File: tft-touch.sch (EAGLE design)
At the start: 4 parts

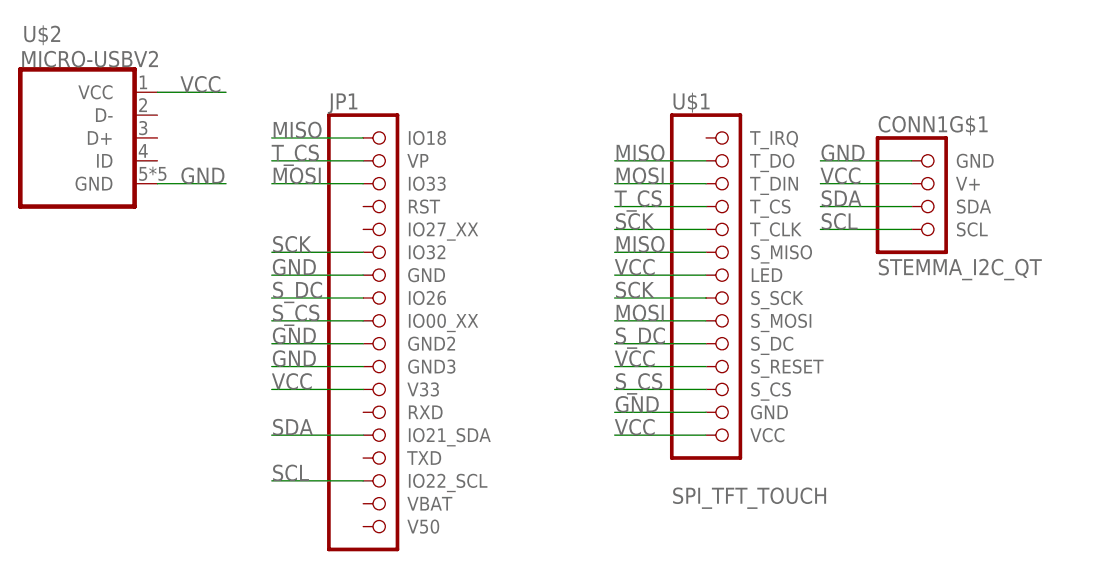
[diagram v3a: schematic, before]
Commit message: Enlarged usb pin holes
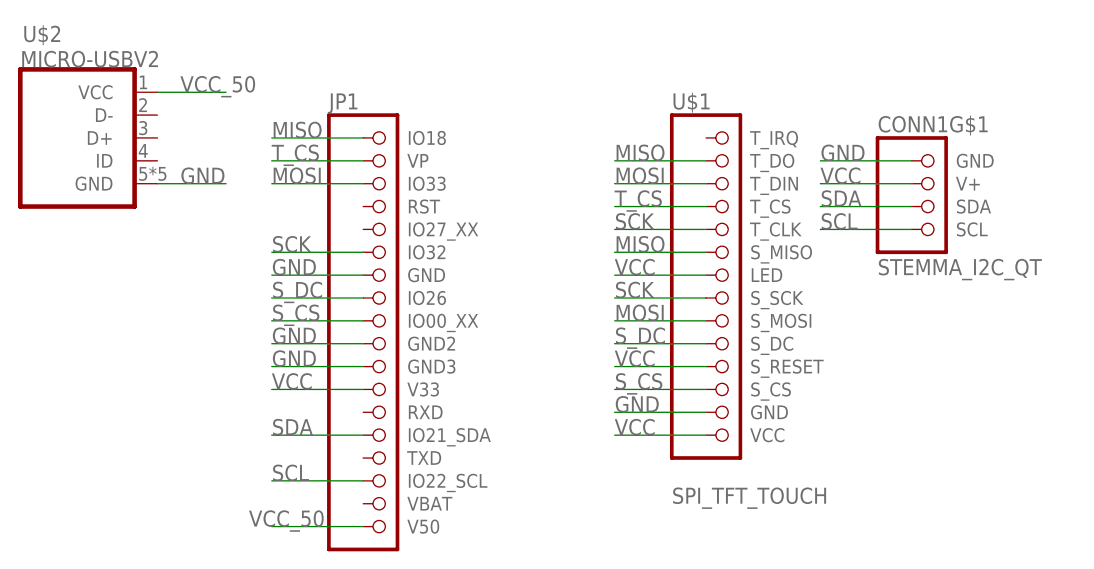
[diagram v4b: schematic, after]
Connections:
- new net VCC_50: JP1.V50, U$2.VCC
- net VCC: no longer U$2.VCC

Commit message: Fix USB connector dimensions
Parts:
- U$2: device microusb:MICRO-USBV2 -> 01jim:MICRO-USBV2
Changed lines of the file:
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@@
 <grid distance="0.1" unitdist="inch" unit="inch" style="lines" multiple="1" display="no" altdistance="0.01" altunitdist="inch" altunit="inch"/>
 <layers>
-<layer number="1" name="Top" color="4" fill="1" visible="yes" active="no"/>
-<layer number="16" name="Bottom" color="1" fill="1" visible="yes" active="no"/>
-<layer number="17" name="Pads" color="2" fill="1" visible="yes" active="no"/>
-<layer number="18" name="Vias" color="2" fill="1" visible="yes" active="no"/>
-<layer number="19" name="Unrouted" color="6" fill="1" visible="yes" active="no"/>
-<layer number="20" name="Dimension" color="24" fill="1" visible="yes" active="no"/>
-<layer number="21" name="tPlace" color="7" fill="1" visible="yes" active="no"/>
-<layer number="22" name="bPlace" color="7" fill="1" visible="yes" active="no"/>
-<layer number="23" name="tOrigins" color="15" fill="1" visible="yes" active="no"/>
-<layer number="24" name="bOrigins" color="15" fill="1" visible="yes" active="no"/>
-<layer number="25" name="tNames" color="7" fill="1" visible="yes" active="no"/>
-<layer number="26" name="bNames" color="7" fill="1" visible="yes" active="no"/>
-<layer number="27" name="tValues" color="7" fill="1" visible="yes" active="no"/>
-<layer number="28" name="bValues" color="7" fill="1" visible="yes" active="no"/>
+<layer number="1" name="Top" color="4" fill="1" visible="no" active="no"/>
+<layer number="16" name="Bottom" color="1" fill="1" visible="no" active="no"/>
+<layer number="17" name="Pads" color="2" fill="1" visible="no" active="no"/>
+<layer number="18" name="Vias" color="2" fill="1" visible="no" active="no"/>
+<layer number="19" name="Unrouted" color="6" fill="1" visible="no" active="no"/>
+<layer number="20" name="Dimension" color="24" fill="1" visible="no" active="no"/>
+<layer number="21" name="tPlace" color="7" fill="1" visible="no" active="no"/>
+<layer number="22" name="bPlace" color="7" fill="1" visible="no" active="no"/>
+<layer number="23" name="tOrigins" color="15" fill="1" visible="no" active="no"/>
+<layer number="24" name="bOrigins" color="15" fill="1" visible="no" active="no"/>
+<layer number="25" name="tNames" color="7" fill="1" visible="no" active="no"/>
+<layer number="26" name="bNames" color="7" fill="1" visible="no" active="no"/>
+<layer number="27" name="tValues" color="7" fill="1" visible="no" active="no"/>
+<layer number="28" name="bValues" color="7" fill="1" visible="no" active="no"/>
 <layer number="29" name="tStop" color="7" fill="3" visible="no" active="no"/>
 <layer number="30" name="bStop" color="7" fill="6" visible="no" active="no"/>
@@
 <layer number="35" name="tGlue" color="7" fill="4" visible="no" active="no"/>
 <layer number="36" name="bGlue" color="7" fill="5" visible="no" active="no"/>
-<layer number="37" name="tTest" color="7" fill="1" visible="yes" active="no"/>
-<layer number="38" name="bTest" color="7" fill="1" visible="yes" active="no"/>
+<layer number="37" name="tTest" color="7" fill="1" visible="no" active="no"/>
+<layer number="38" name="bTest" color="7" fill="1" visible="no" active="no"/>
 <layer number="39" name="tKeepout" color="4" fill="11" visible="no" active="no"/>
 <layer number="40" name="bKeepout" color="1" fill="11" visible="no" active="no"/>
@@
 <layer number="44" name="Drills" color="7" fill="1" visible="no" active="no"/>
 <layer number="45" name="Holes" color="7" fill="1" visible="no" active="no"/>
-<layer number="46" name="Milling" color="3" fill="1" visible="yes" active="no"/>
-<layer number="47" name="Measures" color="7" fill="1" visible="yes" active="no"/>
-<layer number="48" name="Document" color="7" fill="1" visible="yes" active="no"/>
-<layer number="49" name="Reference" color="7" fill="1" visible="yes" active="no"/>
-<layer number="50" name="dxf" color="7" fill="1" visible="yes" active="no"/>
-<layer number="51" name="tDocu" color="7" fill="1" visible="yes" active="no"/>
-<layer number="52" name="bDocu" color="7" fill="1" visible="yes" active="no"/>
-<layer number="53" name="tGND_GNDA" color="7" fill="9" visible="yes" active="no"/>
-<layer number="54" name="bGND_GNDA" color="1" fill="9" visible="yes" active="no"/>
-<layer number="56" name="wert" color="7" fill="1" visible="yes" active="no"/>
-<layer number="57" name="tCAD" color="7" fill="1" visible="yes" active="no"/>
-<layer number="58" name="b3D" color="7" fill="1" visible="yes" active="no"/>
-<layer number="59" name="tCarbon" color="7" fill="1" visible="yes" active="no"/>
-<layer number="60" name="bCarbon" color="7" fill="1" visible="yes" active="no"/>
-<layer number="61" name="stand" color="7" fill="1" visible="yes" active="no"/>
+<layer number="46" name="Milling" color="3" fill="1" visible="no" active="no"/>
+<layer number="47" name="Measures" color="7" fill="1" visible="no" active="no"/>
+<layer number="48" name="Document" color="7" fill="1" visible="no" active="no"/>
+<layer number="49" name="Reference" color="7" fill="1" visible="no" active="no"/>
+<layer number="50" name="dxf" color="7" fill="1" visible="no" active="no"/>
+<layer number="51" name="tDocu" color="7" fill="1" visible="no" active="no"/>
+<layer number="52" name="bDocu" color="7" fill="1" visible="no" active="no"/>
+<layer number="53" name="tGND_GNDA" color="7" fill="9" visible="no" active="no"/>
+<layer number="54" name="bGND_GNDA" color="1" fill="9" visible="no" active="no"/>
+<layer number="56" name="wert" color="7" fill="1" visible="no" active="no"/>
+<layer number="57" name="tCAD" color="7" fill="1" visible="no" active="no"/>
+<layer number="58" name="b3D" color="7" fill="1" visible="no" active="no"/>
+<layer number="59" name="tCarbon" color="7" fill="1" visible="no" active="no"/>
+<layer number="60" name="bCarbon" color="7" fill="1" visible="no" active="no"/>
+<layer number="61" name="stand" color="7" fill="1" visible="no" active="no"/>
 <layer number="88" name="SimResults" color="9" fill="1" visible="yes" active="yes"/>
 <layer number="89" name="SimProbes" color="9" fill="1" visible="yes" active="yes"/>
@@
 <part name="JP1" library="00jim" deviceset="TTGO-TS-ESP32" device=""/>
 <part name="CONN1" library="00jim" deviceset="STEMMA_I2C" device="_QT"/>
-<part name="U$2" library="microusb" deviceset="MICRO-USB" device="V2" value="MICRO-USBV2"/>
+<part name="U$2" library="01jim" deviceset="MICRO-USB" device="V2" value="MICRO-USBV2"/>
 </parts>
 <sheets>
